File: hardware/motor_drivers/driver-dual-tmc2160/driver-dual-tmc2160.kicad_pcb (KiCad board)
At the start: 4 copper layers, 30 x 33.5 mm, 74 parts, among them M1 Micro-Fit 3.0, M2 Micro-Fit 3.0, Q1 DMHT6016LFJ, Q2 DMHT6016LFJ, Q3 DMHT6016LFJ, Q4 DMHT6016LFJ, T1 GND, T10 SCK, T11 GND, T12 DIR, T13 ENCB, T14 SDI, T15 EN, T16 ENCN, T17 SDO, T18 VCC, T2 CS0, T21 Therm, T3 DIAG0, T4 CLK, T5 STEP, T6 DIAG1, T7 12V, T8 GND, T9 ENCA, U1 TMC2160, U2 TMC2160

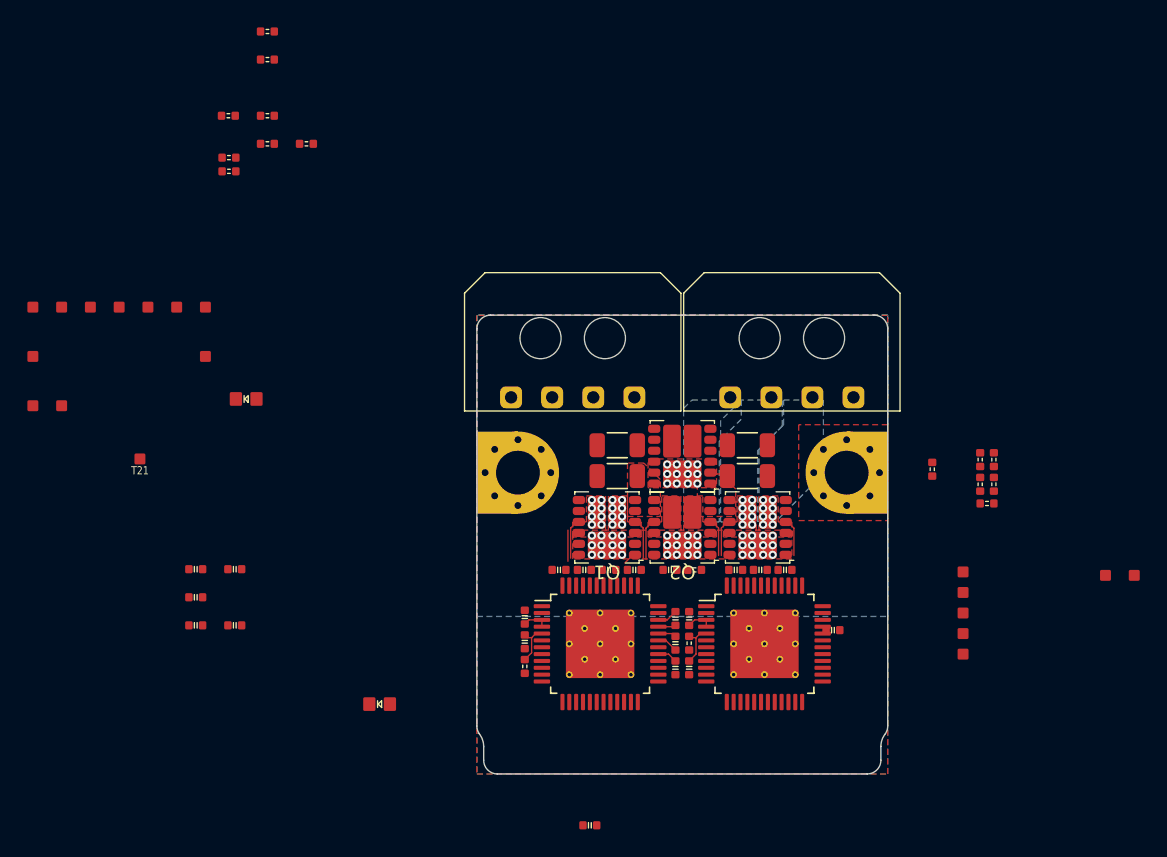
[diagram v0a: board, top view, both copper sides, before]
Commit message: added ctb v0.3 and dual 2160, fixed typo in v0.6 manual
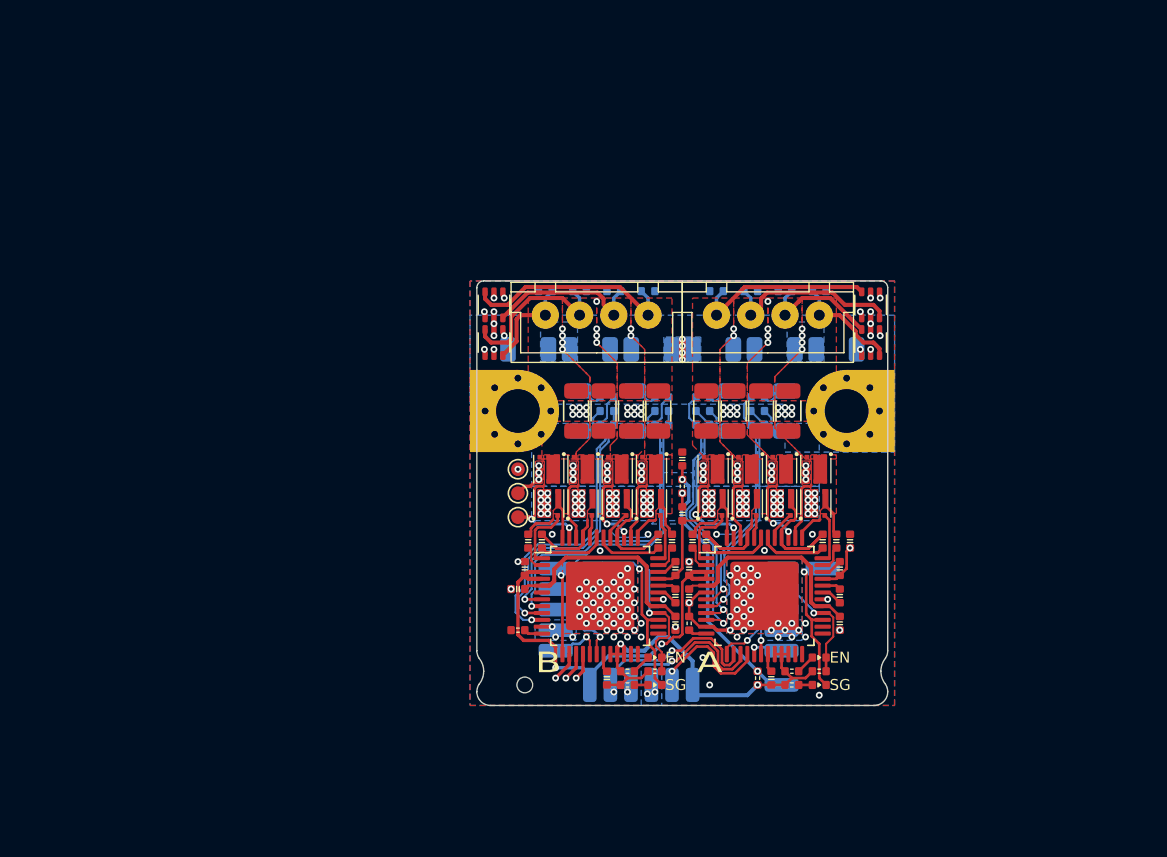
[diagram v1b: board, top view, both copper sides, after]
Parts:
- removed M1, M2: Micro-Fit 3.0, corevus:XKB_X3025WR-04
- removed T21: Therm, corevus:LGA_Land
- added C23: 100nF 100V, PCM_ME_passives:0402C, F.Cu at (134.5, 73.5)
- added C24: 1μF, PCM_ME_passives:0402C, F.Cu at (123.0, 73.0)
- added C25: 1µF, PCM_ME_passives:0402C, F.Cu at (134.5, 75.5)
- added C26: 1µF, PCM_ME_passives:0402C, F.Cu at (129.5, 79.5)
- added C27: 1μF, PCM_ME_passives:0402C, F.Cu at (123.5, 71.5)
- added C28: 100nF 100V, PCM_ME_passives:0402C, F.Cu at (135.0, 67.5)
- added C29: 1μF 25V, PCM_ME_passives:0402C, F.Cu at (123.8, 69.5)
- added C30: 1μF 25V, PCM_ME_passives:0402C, F.Cu at (124.8, 69.5)
- added C31: 1μF 25V, PCM_ME_passives:0402C, F.Cu at (133.2, 69.5)
- added C32: 1μF 25V, PCM_ME_passives:0402C, F.Cu at (134.2, 69.5)
- added C33: 1nF, PCM_ME_passives:0402C, B.Cu at (129.5, 61.0)
- added C34: 1nF 100V, PCM_ME_passives:0402C, B.Cu at (132.5, 51.2)
- added C35: 1nF 100V, PCM_ME_passives:0402C, B.Cu at (130.0, 51.2)
- added C36: 1nF 100V, PCM_ME_passives:0402C, B.Cu at (127.5, 51.2)
- added C37: 1nF 100V, PCM_ME_passives:0402C, B.Cu at (125.0, 51.2)
- added C38: 1μF 100V, Capacitor_SMD:C_1206_3216Metric, B.Cu at (137.2, 55.5)
- added C39: 1μF 100V, Capacitor_SMD:C_1206_3216Metric, B.Cu at (141.8, 55.5)
- added C40: 1μF 100V, Capacitor_SMD:C_1206_3216Metric, B.Cu at (146.2, 55.5)
- added C41: 1nF, PCM_ME_passives:0402C, B.Cu at (133.5, 61.0)
- added D3: BAV99S, Package_TO_SOT_SMD:SOT-363_SC-70-6, F.Cu at (148.8, 52.2)
- added D4: BAV99S, Package_TO_SOT_SMD:SOT-363_SC-70-6, F.Cu at (148.8, 55.0)
- added D5: Blu, PCM_ME_passives:0402LED, F.Cu at (133.0, 78.0)
- added D6: Ylw, PCM_ME_passives:0402LED, F.Cu at (133.0, 80.0)
- added D7: BAV99S, Package_TO_SOT_SMD:SOT-363_SC-70-6, F.Cu at (121.2, 52.2)
- added D8: BAV99S, Package_TO_SOT_SMD:SOT-363_SC-70-6, F.Cu at (121.2, 55.0)
- added FB1: 30Ω@100MHz, Resistor_SMD:R_1206_3216Metric, F.Cu at (142.8, 60.0)
- added FB2: 30Ω@100MHz, Resistor_SMD:R_1206_3216Metric, F.Cu at (140.8, 60.0)
- added FB3: 30Ω@100MHz, Resistor_SMD:R_1206_3216Metric, F.Cu at (138.8, 60.0)
- added FB4: 30Ω@100MHz, Resistor_SMD:R_1206_3216Metric, F.Cu at (136.8, 60.0)
- added FB5: 30Ω@100MHz, Resistor_SMD:R_1206_3216Metric, F.Cu at (133.2, 60.0)
- added FB6: 30Ω@100MHz, Resistor_SMD:R_1206_3216Metric, F.Cu at (131.2, 60.0)
- added FB7: 30Ω@100MHz, Resistor_SMD:R_1206_3216Metric, F.Cu at (129.2, 60.0)
- added FB8: 30Ω@100MHz, Resistor_SMD:R_1206_3216Metric, F.Cu at (127.2, 60.0)
- added H3: ToolingHole, corevus:ToolingHole, F.Cu at (123.5, 80.0)
- added J1: XH, corevus:JST_XH_1x04, F.Cu at (141.2, 53.0)
- added J2: XH, corevus:JST_XH_1x04, F.Cu at (128.8, 53.0)
- added NT1: NetTie_2, corevus:NetTie-2_SMD_Pad0.1mm, B.Cu at (137.8, 58.9)
- added NT2: NetTie_2, corevus:NetTie-2_SMD_Pad0.1mm, B.Cu at (141.8, 58.9)
- added NT3: NetTie_2, corevus:NetTie-2_SMD_Pad0.1mm, B.Cu at (128.2, 58.9)
- added NT4: NetTie_2, corevus:NetTie-2_SMD_Pad0.1mm, B.Cu at (132.2, 58.9)
- added Q10: DMT6016, corevus:DMT6016LFDF, F.Cu at (125.2, 64.2)
- added Q11: DMT6016, corevus:DMT6016LFDF, F.Cu at (127.8, 66.8)
- added Q12: DMT6016, corevus:DMT6016LFDF, F.Cu at (127.8, 64.2)
- added Q13: DMT6016, corevus:DMT6016LFDF, F.Cu at (130.2, 66.8)
- added Q14: DMT6016, corevus:DMT6016LFDF, F.Cu at (130.2, 64.2)
- added Q15: DMT6016, corevus:DMT6016LFDF, F.Cu at (132.8, 66.8)
- added Q16: DMT6016, corevus:DMT6016LFDF, F.Cu at (132.8, 64.2)
- added Q5: DMT6016, corevus:DMT6016LFDF, F.Cu at (142.2, 66.8)
- added Q6: DMT6016, corevus:DMT6016LFDF, F.Cu at (142.2, 64.2)
- added Q7: DMT6016, corevus:DMT6016LFDF, F.Cu at (144.8, 66.8)
- added Q8: DMT6016, corevus:DMT6016LFDF, F.Cu at (144.8, 64.2)
- added Q9: DMT6016, corevus:DMT6016LFDF, F.Cu at (125.2, 66.8)
- added R21: 47Ω, PCM_ME_passives:0402R, B.Cu at (133.5, 59.0)
- added T19: EN, corevus:LGA_Land_2.5mm, B.Cu at (125.8, 73.0)
- added TP1: TestPoint, TestPoint:TestPoint_Pad_D1.0mm, F.Cu at (123.0, 64.2)
- added TP5: TestPoint, TestPoint:TestPoint_Pad_D1.0mm, F.Cu at (123.0, 67.8)
- added TP6: TestPoint, TestPoint:TestPoint_Pad_D1.0mm, F.Cu at (123.0, 66.0)
- C1: value 100nF 16V -> 1μF 25V; footprint AlphaLib:0402C -> PCM_ME_passives:0402C
- C10, C11, C22, C8, C9: value 1μF -> 1μF 25V; footprint AlphaLib:0402C -> PCM_ME_passives:0402C
- C12: value 100nF 16V -> 1μF 100V; footprint AlphaLib:0402C -> Capacitor_SMD:C_1206_3216Metric; moved to B.Cu
- C13: value 22nF 100V -> 1μF; footprint AlphaLib:0402C -> PCM_ME_passives:0402C
- C14: value 1µF -> 1μF 100V; footprint AlphaLib:0402C -> Capacitor_SMD:C_1206_3216Metric; moved to B.Cu
- C15: value 1μF -> 1μF 100V; footprint AlphaLib:0402C -> Capacitor_SMD:C_1206_3216Metric; moved to B.Cu
- C16: value 1µF -> 1nF 100V; footprint AlphaLib:0402C -> PCM_ME_passives:0402C; moved to B.Cu
- C17, C19: value 1μF -> 1nF 100V; footprint AlphaLib:0402C -> PCM_ME_passives:0402C; moved to B.Cu
- C18: value 100nF 100V -> 1nF 100V; footprint AlphaLib:0402C -> PCM_ME_passives:0402C; moved to B.Cu
- C2: value 22nF 100V -> 100nF 100V; footprint AlphaLib:0402C -> PCM_ME_passives:0402C
- C20, C21: value 1μF -> 1nF; footprint AlphaLib:0402C -> PCM_ME_passives:0402C; moved to B.Cu
- C3, C4, C5, C6, C7: footprint AlphaLib:0402C -> PCM_ME_passives:0402C
- D1: value Red -> Blu; footprint AlphaLib:0603LED -> PCM_ME_passives:0402LED
- D2: value Red -> Ylw; footprint AlphaLib:0603LED -> PCM_ME_passives:0402LED
- Q1, Q2, Q3, Q4: value DMHT6016LFJ -> DMT6016; footprint corevus:V-DFN5045-12-Type-B -> corevus:DMT6016LFDF
- R1: value 1kΩ -> 4.7kΩ; footprint AlphaLib:0402R -> PCM_ME_passives:0402R
- R10, R13, R17: value 30mΩ -> 50mΩ; moved to B.Cu
- R11, R12, R15, R19, R8, R9: footprint AlphaLib:0402R -> PCM_ME_passives:0402R; moved to B.Cu
- R14: value 30mΩ -> 47Ω; footprint Resistor_SMD:R_1206_3216Metric -> PCM_ME_passives:0402R; moved to B.Cu
- R16: value 47Ω -> 1kΩ; footprint AlphaLib:0402R -> PCM_ME_passives:0402R
- R18: value 47Ω -> 50mΩ; footprint AlphaLib:0402R -> Resistor_SMD:R_1206_3216Metric; moved to B.Cu
- R2, R20, R3: footprint AlphaLib:0402R -> PCM_ME_passives:0402R
- R4: value 2.2Ω -> 10kΩ; footprint AlphaLib:0402R -> PCM_ME_passives:0402R
- R5: value 1kΩ -> 10kΩ; footprint AlphaLib:0402R -> PCM_ME_passives:0402R
- R6: value 10kΩ -> 4.7kΩ; footprint AlphaLib:0402R -> PCM_ME_passives:0402R
- R7: value 2.2Ω -> 1kΩ; footprint AlphaLib:0402R -> PCM_ME_passives:0402R
- T1: value GND -> DIAG; footprint corevus:LGA_Land -> corevus:LGA_Land_2.5mm; moved to B.Cu
- T10: value SCK -> CS0; footprint corevus:LGA_Land -> corevus:LGA_Land_2.5mm; moved to B.Cu
- T11: value GND -> STEP; footprint corevus:LGA_Land -> corevus:LGA_Land_2.5mm; moved to B.Cu
- T12: value DIR -> GND; footprint corevus:LGA_Land -> corevus:LGA_Land_2.5mm; moved to B.Cu
- T13: value ENCB -> DIR; footprint corevus:LGA_Land -> corevus:LGA_Land_2.5mm; moved to B.Cu
- T14: value SDI -> EN; footprint corevus:LGA_Land -> corevus:LGA_Land_2.5mm; moved to B.Cu
- T15: value EN -> STEP; footprint corevus:LGA_Land -> corevus:LGA_Land_2.5mm; moved to B.Cu
- T16: value ENCN -> GND; footprint corevus:LGA_Land -> corevus:LGA_Land_2.5mm; moved to B.Cu
- T17: value SDO -> DIAG; footprint corevus:LGA_Land -> corevus:LGA_Land_2.5mm; moved to B.Cu
- T18: value VCC -> DIR; footprint corevus:LGA_Land -> corevus:LGA_Land_2.5mm; moved to B.Cu
- T2: footprint corevus:LGA_Land -> corevus:LGA_Land_2.5mm; moved to B.Cu
- T3: value DIAG0 -> 12V; footprint corevus:LGA_Land -> corevus:LGA_Land_2.5mm; moved to B.Cu
- T4: value CLK -> SCK; footprint corevus:LGA_Land -> corevus:LGA_Land_2.5mm; moved to B.Cu
- T5: value STEP -> GND; footprint corevus:LGA_Land -> corevus:LGA_Land_2.5mm; moved to B.Cu
- T6: value DIAG1 -> SDI; footprint corevus:LGA_Land -> corevus:LGA_Land_2.5mm; moved to B.Cu
- T7: value 12V -> SDO; footprint corevus:LGA_Land -> corevus:LGA_Land_2.5mm; moved to B.Cu
- T8: value GND -> VCC; footprint corevus:LGA_Land -> corevus:LGA_Land_2.5mm; moved to B.Cu
- T9: value ENCA -> Therm; footprint corevus:LGA_Land -> corevus:LGA_Land_2.5mm; moved to B.Cu
- TH1: value 10kΩ 3380K -> 10kΩ 3950K; footprint AlphaLib:0402R -> PCM_ME_passives:0402R
- moved T17 58.9 mm to (145.2, 71.5), turned to -90 degrees
- moved R1 57.8 mm to (143.0, 79.0)
- moved R2 57.1 mm to (145.0, 79.0)
- moved T8 53.8 mm to (135.8, 80.0)
- moved R6 51.8 mm to (131.0, 79.0)
- moved R5 47.4 mm to (123.0, 76.0), turned to 180 degrees
- moved C16 47.3 mm to (145.0, 51.2), turned to 180 degrees
- moved R3 47.1 mm to (135.5, 75.5), turned to 90 degrees
- moved T5 46.0 mm to (132.8, 80.0)
- moved D1 45.9 mm to (145.0, 78.0), turned to 180 degrees
- moved T3 45.7 mm to (128.2, 80.0)
- moved T1 45.4 mm to (128.8, 71.5), turned to -90 degrees
- moved T4 45.2 mm to (129.8, 80.0)
- moved C18 44.9 mm to (140.0, 51.2), turned to 180 degrees
- moved T7 43.8 mm to (134.2, 80.0)
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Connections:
- C10 pad 2: /_{M0}A1 -> /_{MA}A1
- C11 pad 2: /_{M0}A2 -> /_{MA}A2
- C12 pad 1: Net-(U2-VCP) -> +48V
- C12 pad 2: +48V -> GND
- C13 pad 1: Net-(U2-CPO) -> /THERM
- C13 pad 2: Net-(U2-CPI) -> GND
- C14 pad 1: GND -> +48V
- C14 pad 2: VCC -> GND
- C15 pad 1: GND -> +48V
- C15 pad 2: Net-(U2-5VOUT) -> GND
- C16 pad 2: Net-(U2-VCC) -> /_{MA}A2'
- C17 pad 1: +12V -> GND
- C17 pad 2: GND -> /_{MA}A1'
- C18 pad 1: +48V -> GND
- C18 pad 2: GND -> /_{MA}B2'
- C19 pad 1: Net-(U2-CB1) -> GND
- C19 pad 2: /_{M1}B1 -> /_{MA}B1'
- C20 pad 1: Net-(U2-CB2) -> /_{MA}SRBL
- C20 pad 2: /_{M1}B2 -> /_{MA}SRBH
- C21 pad 1: Net-(U2-CA1) -> /_{MA}SRAL
- C21 pad 2: /_{M1}A1 -> /_{MA}SRAH
- C22 pad 1: Net-(U2-CA2) -> Net-(U2-VCP)
- C22 pad 2: /_{M1}A2 -> +48V
- C5 pad 2: Net-(U1-VCC) -> Net-(U1-5VOUT)
- C8 pad 2: /_{M0}B1 -> /_{MA}B1
- C9 pad 2: /_{M0}B2 -> /_{MA}B2
- D1 pad 1: Net-(D1-K) -> /_{MA}~{En}
- D1 pad 2: VCC -> Net-(D1-A)
- D2 pad 1: Net-(D2-K) -> /_{MA}Stall
- D2 pad 2: VCC -> Net-(D2-A)
- Q1 pad 1: /_{M0}HA1 -> +48V
- Q1 pad 3: /_{M0}A1 -> /_{MA}HB1
- Q1 pad 4: /_{M0}LA1 -> /_{MA}B1
- Q1 pad 5: Net-(Q1-S2-Pad5) -> +48V
- Q1 pad 6: Net-(Q1-S2-Pad5) -> +48V
- Q1 pad 7: Net-(Q1-S3-Pad7) -> /_{MA}B1
- Q1 pad 8: Net-(Q1-S3-Pad7) -> +48V
- Q2 pad 1: /_{M1}HB1 -> /_{MA}B1
- Q2 pad 2: +48V -> /_{MA}B1
- Q2 pad 3: /_{M1}B1 -> /_{MA}LB1
- Q2 pad 4: /_{M1}LB1 -> Net-(Q2-S-Pad4)
- Q2 pad 5: Net-(Q2-S2-Pad5) -> /_{MA}B1
- Q2 pad 6: Net-(Q2-S2-Pad5) -> /_{MA}B1
- Q2 pad 7: Net-(Q1-S2-Pad5) -> Net-(Q2-S-Pad4)
- Q2 pad 8: Net-(Q1-S2-Pad5) -> /_{MA}B1
- Q3 pad 1: /_{M1}HA2 -> +48V
- Q3 pad 3: /_{M1}A2 -> /_{MA}HB2
- Q3 pad 4: /_{M1}LA2 -> /_{MA}B2
- Q3 pad 5: Net-(Q3-S2-Pad5) -> +48V
- Q3 pad 6: Net-(Q3-S2-Pad5) -> +48V
- Q3 pad 7: Net-(Q1-S3-Pad7) -> /_{MA}B2
- Q3 pad 8: Net-(Q1-S3-Pad7) -> +48V
- Q4 pad 1: /_{M1}HA1 -> /_{MA}B2
- Q4 pad 2: +48V -> /_{MA}B2
- Q4 pad 3: /_{M1}A1 -> /_{MA}LB2
- Q4 pad 4: /_{M1}LA1 -> Net-(Q2-S-Pad4)
- Q4 pad 5: Net-(Q3-S2-Pad5) -> /_{MA}B2
- Q4 pad 6: Net-(Q3-S2-Pad5) -> /_{MA}B2
- Q4 pad 7: Net-(Q2-S2-Pad5) -> Net-(Q2-S-Pad4)
- Q4 pad 8: Net-(Q2-S2-Pad5) -> /_{MA}B2
- R1 pad 1: Net-(D1-K) -> VCC
- R1 pad 2: /_{M0}~{En} -> Net-(D1-A)
- R10 pad 1: Net-(Q1-S3-Pad7) -> Net-(Q2-S-Pad4)
- R11 pad 1: Net-(Q1-S2-Pad5) -> Net-(Q6-S-Pad4)
- R11 pad 2: /_{M0}SRAH -> /_{MA}SRAH
- R12 pad 1: GND -> Net-(NT2-Pad2)
- R12 pad 2: /_{M0}SRAL -> /_{MA}SRAL
- R13 pad 1: Net-(Q1-S2-Pad5) -> Net-(Q6-S-Pad4)
- R14 pad 1: Net-(Q2-S2-Pad5) -> Net-(Q10-S-Pad4)
- R14 pad 2: GND -> /_{MB}SRBH
- R15 pad 1: Net-(Q2-S2-Pad5) -> Net-(NT3-Pad1)
- R15 pad 2: /_{M1}SRBH -> /_{MB}SRBL
- R16 pad 1: GND -> VCC
- R16 pad 2: /_{M1}SRBL -> Net-(D2-A)
- R17 pad 1: Net-(Q3-S2-Pad5) -> Net-(Q10-S-Pad4)
- R18 pad 1: Net-(Q3-S2-Pad5) -> Net-(Q14-S-Pad4)
- R18 pad 2: /_{M1}SRAH -> GND
- R19 pad 1: GND -> Net-(Q14-S-Pad4)
- R19 pad 2: /_{M1}SRAL -> /_{MB}SRAH
- R2 pad 2: /_{M0}~{En} -> /_{MA}~{En}
- R3 pad 1: /Clk -> Net-(U1-CLK)
- R4 pad 1: Net-(U1-5VOUT) -> VCC
- R4 pad 2: Net-(U1-VCC) -> /_{MB}~{En}
- R5 pad 1: Net-(D2-K) -> Net-(U2-CLK)
- R5 pad 2: /_{M1}~{En} -> GND
- R6 pad 2: /_{M1}~{En} -> Net-(D5-A)
- R7 pad 1: Net-(U2-5VOUT) -> VCC
- R7 pad 2: Net-(U2-VCC) -> Net-(D6-A)
- R8 pad 1: Net-(Q1-S3-Pad7) -> Net-(Q2-S-Pad4)
- R8 pad 2: /_{M0}SRBH -> /_{MA}SRBH
- R9 pad 1: GND -> Net-(NT1-Pad1)
- R9 pad 2: /_{M0}SRBL -> /_{MA}SRBL
- T1 pad 1: GND -> /_{MB}Stall
- T10 pad 1: /SCK -> /_{MA}~{CS}
- T11 pad 1: GND -> /_{MA}Step
- T12 pad 1: /Dir -> GND
- T13 pad 1: /ENCB -> /_{MA}Dir
- T14 pad 1: /SDI -> /_{MA}~{En}
- T15 pad 1: /~{En} -> /_{MB}Step
- T16 pad 1: /ENCN -> GND
- T17 pad 1: /SDO -> /_{MA}Stall
- T18 pad 1: VCC -> /_{MB}Dir
- T2 pad 1: /~{CS} -> /_{MB}~{CS}
- T3 pad 1: /Diag0 -> +12V
- T4 pad 1: /Clk -> /SCK
- T5 pad 1: /Step -> GND
- T6 pad 1: /Diag1 -> /SDI
- T7 pad 1: +12V -> /SDO
- T8 pad 1: GND -> VCC
- T9 pad 1: /ENCA -> /THERM
- U1 pad 1: /_{M0}HB1 -> /_{MA}HB1
- U1 pad 10: /_{M0}SRBL -> /_{MA}SRBL
- U1 pad 12: /Clk -> Net-(U1-CLK)
- U1 pad 13: /~{CS} -> /_{MA}~{CS}
- U1 pad 17: /_{M0}Step -> /_{MA}Step
- U1 pad 18: /_{M0}Dir -> /_{MA}Dir
- U1 pad 26: /_{M0}Stall -> unconnected-(U1-DIAG0-Pad26)
- U1 pad 27: unconnected-(U1-DIAG1-Pad27) -> /_{MA}Stall
- U1 pad 28: /_{M0}~{En} -> /_{MA}~{En}
- U1 pad 29: Net-(U1-VCC) -> Net-(U1-5VOUT)
- U1 pad 36: /_{M0}HA2 -> /_{MA}HA2
- U1 pad 37: /_{M0}A2 -> /_{MA}A2
- U1 pad 38: /_{M0}LA2 -> /_{MA}LA2
- U1 pad 39: /_{M0}LA1 -> /_{MA}LA1
- U1 pad 40: /_{M0}A1 -> /_{MA}A1
- U1 pad 41: /_{M0}HA1 -> /_{MA}HA1
- U1 pad 44: /_{M0}HB2 -> /_{MA}HB2
- U1 pad 45: /_{M0}B2 -> /_{MA}B2
- U1 pad 46: /_{M0}LB2 -> /_{MA}LB2
- U1 pad 47: /_{M0}LB1 -> /_{MA}LB1
- U1 pad 48: /_{M0}B1 -> /_{MA}B1
- U1 pad 7: /_{M0}SRAL -> /_{MA}SRAL
- U1 pad 8: /_{M0}SRAH -> /_{MA}SRAH
- U1 pad 9: /_{M0}SRBH -> /_{MA}SRBH
- U2 pad 1: /_{M1}HB1 -> /_{MB}HB1
- U2 pad 10: /_{M1}SRBL -> /_{MB}SRBL
- U2 pad 12: /Clk -> Net-(U2-CLK)
- U2 pad 13: /~{CS} -> /_{MB}~{CS}
- U2 pad 17: /_{M1}Step -> /_{MB}Step
- U2 pad 18: /_{M1}Dir -> /_{MB}Dir
- U2 pad 26: /_{M1}Stall -> unconnected-(U2-DIAG0-Pad26)
- U2 pad 27: unconnected-(U2-DIAG1-Pad27) -> /_{MB}Stall
- U2 pad 28: /_{M1}~{En} -> /_{MB}~{En}
- U2 pad 29: Net-(U2-VCC) -> Net-(U2-5VOUT)
- U2 pad 36: /_{M1}HA2 -> /_{MB}HA2
- U2 pad 37: /_{M1}A2 -> /_{MB}A2
- U2 pad 38: /_{M1}LA2 -> /_{MB}LA2
- U2 pad 39: /_{M1}LA1 -> /_{MB}LA1
- U2 pad 40: /_{M1}A1 -> /_{MB}A1
- U2 pad 41: /_{M1}HA1 -> /_{MB}HA1
- U2 pad 44: /_{M1}HB2 -> /_{MB}HB2
- U2 pad 45: /_{M1}B2 -> /_{MB}B2
- U2 pad 46: /_{M1}LB2 -> /_{MB}LB2
- U2 pad 47: /_{M1}LB1 -> /_{MB}LB1
- U2 pad 48: /_{M1}B1 -> /_{MB}B1
- U2 pad 7: /_{M1}SRAL -> /_{MB}SRAL
- U2 pad 8: /_{M1}SRAH -> /_{MB}SRAH
- U2 pad 9: /_{M1}SRBH -> /_{MB}SRBH
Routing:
- net VCC: track 0.00 -> 29.3 mm, vias 0 -> 2
- net +12V: track 3.79 -> 31.0 mm, vias 0 -> 2
- net /_{MB}SRAL: track 0.00 -> 24.9 mm, vias 0 -> 1
- net /_{MB}SRAH: track 0.00 -> 23.4 mm, vias 0 -> 1
- net /_{MB}SRBL: track 0.00 -> 23.0 mm, vias 0 -> 1
- net /_{MB}SRBH: track 0.00 -> 20.8 mm, vias 0 -> 1
- net /_{MA}SRBL: track 0.00 -> 20.0 mm, vias 0 -> 1
- net /THERM: track 0.00 -> 19.9 mm, vias 0 -> 2
- net GND: track 0.00 -> 19.3 mm, vias 0 -> 137
- net /SCK: track 0.00 -> 18.9 mm, vias 0 -> 3
- net /SDO: track 0.00 -> 18.5 mm, vias 0 -> 2
- net /SDI: track 0.00 -> 18.1 mm, vias 0 -> 3
- net /_{MA}SRBH: track 0.00 -> 17.9 mm, vias 0 -> 1
- net /_{MB}~{En}: track 0.00 -> 17.6 mm, vias 0 -> 1
- net /_{MA}SRAL: track 0.00 -> 17.3 mm, vias 0 -> 1
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- added copper zone on In2.Cu, net +48V
- added copper zone on In3.Cu, net +48V
- added copper zone on F.Cu, net /_{MA}A1
- added copper zone on F.Cu, net /_{MA}A1'
- added copper zone on F.Cu, net /_{MA}A2
- added copper zone on F.Cu, net /_{MA}A2'
- added copper zone on F.Cu, net /_{MA}B1
- added copper zone on F.Cu, net /_{MA}B1'
- added copper zone on F.Cu, net /_{MA}B2
- added copper zone on F.Cu, net /_{MA}B2'
- added copper zone on F.Cu, net /_{MB}A1
- added copper zone on F.Cu, net /_{MB}A1'
- added copper zone on F.Cu, net /_{MB}A2
- added copper zone on F.Cu, net /_{MB}A2'
- added copper zone on F.Cu, net /_{MB}B1
- added copper zone on F.Cu, net /_{MB}B1'
- added copper zone on F.Cu, net /_{MB}B2
- added copper zone on F.Cu, net /_{MB}B2'
- added copper zone on In3.Cu, net GND
- added copper zone on In4.Cu, net GND
- added copper zone on B.Cu, net Net-(Q10-S-Pad4)
- added copper zone on F.Cu, net Net-(Q10-S-Pad4)
- added copper zone on B.Cu, net Net-(Q14-S-Pad4)
- added copper zone on F.Cu, net Net-(Q14-S-Pad4)
- added copper zone on B.Cu, net Net-(Q2-S-Pad4)
- added copper zone on F.Cu, net Net-(Q2-S-Pad4)
- added copper zone on B.Cu, net Net-(Q6-S-Pad4)
- added copper zone on F.Cu, net Net-(Q6-S-Pad4)
- removed copper zone on F.Cu, net +48V
- removed copper zone on F.Cu, net /_{M0}A1
- removed copper zone on F.Cu, net /_{M0}A2
- removed copper zone on F.Cu, net /_{M0}B2
- removed copper zone on B.Cu, net /_{M1}A1
- removed copper zone on F.Cu, net /_{M1}A1
- removed copper zone on B.Cu, net /_{M1}B1
- removed copper zone on F.Cu, net /_{M1}B1
- removed copper zone on B.Cu, net /_{M1}B2
- removed copper zone on F.Cu, net /_{M1}B2
- removed copper zone on F.Cu, net Net-(Q1-S2-Pad5)
- removed copper zone on F.Cu, net Net-(Q2-S2-Pad5)
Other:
- board size 30 x 33.5 mm -> 30 x 31 mm
- copper layers 4 -> 6
- board text added: "12V"
- board text added: "3V3"
- board text added: "A"
- board text added: "B"
- board text added: "CS"
- board text added: "DIR"
- board text added: "EN"
- board text added: "GND"
- board text added: "MISO"
- board text added: "MOSI"
- board text added: "NOT FOR PRODUCTION USE MERIDI ENGINEERING JULY 2024 DUAL TMC2160 STEPPER DRIVER MODULE 48V MAX / ???Arms MAX PER DRIVER"
- board text added: "SCLK"
- board text added: "SG"
- board text added: "STALL"
- board text added: "STEP"
- board text added: "THERM"

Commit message: last before i go on v0.7
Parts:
- removed H3: ToolingHole, corevus:ToolingHole
- added H4: ToolingHole, corevus:ToolingHole, F.Cu at (0.65, 0.65)
- D1, D5: value Blu -> Grn
- moved C17 5.15 mm to (147.5, 52.5), turned to 180 degrees
- moved C36 5.15 mm to (122.5, 52.5), turned to 0 degrees
- moved C18 4.25 mm to (140.0, 55.5), turned to 90 degrees
- moved C35 4.25 mm to (130.0, 55.5), turned to 90 degrees
- moved C16 3.36 mm to (147.5, 53.5)
- moved C19 3.36 mm to (135.0, 53.5)
- moved C37 3.36 mm to (122.5, 53.5)
- moved C34 2.80 mm to (135.0, 52.5)
- moved C12 1.00 mm to (122.8, 55.5)
- moved C14 1.00 mm to (127.2, 55.5)
- moved C39 1.00 mm to (142.8, 55.5)
- moved C40 1.00 mm to (147.2, 55.5)
- moved C1 0.25 mm to (146.5, 71.8)
- moved C10 0.25 mm to (145.2, 69.8)
- moved C11 0.25 mm to (146.2, 69.8)
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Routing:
- net GND: track 19.3 -> 8.31 mm, vias 137 -> 139
- net /_{MA}A1': track 9.03 -> 12.4 mm
- net /_{MB}B1': track 7.25 -> 3.86 mm
- net /_{MB}B2': track 12.4 -> 15.3 mm
- net /_{MA}A2': track 8.03 -> 5.42 mm
- net /_{MB}~{En}: track 17.6 -> 15.5 mm
- net /_{MA}Stall: track 10.1 -> 11.6 mm
- net +48V: track 17.9 -> 19.1 mm, vias 87 -> 83
- net /_{MB}A1': track 10.7 -> 11.8 mm
- net /_{MA}B2': track 12.6 -> 13.3 mm
- net /_{MB}~{CS}: track 5.79 -> 6.53 mm
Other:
- board text added: "DUAL TMC2160 48V xA EVALUATION USE ONLY"
- board text added: "NOT FOR PRODUCTION USE MERIDI ENGINEERING JULY 2024 DUAL TMC2160 STEPPER DRIVER MODULE 48V MAX xArms MAX PER DRIVER"
- board text added: "corevus"
- board text removed: "NOT FOR PRODUCTION USE MERIDI ENGINEERING JULY 2024 DUAL TMC2160 STEPPER DRIVER MODULE 48V MAX / ???Arms MAX PER DRIVER"

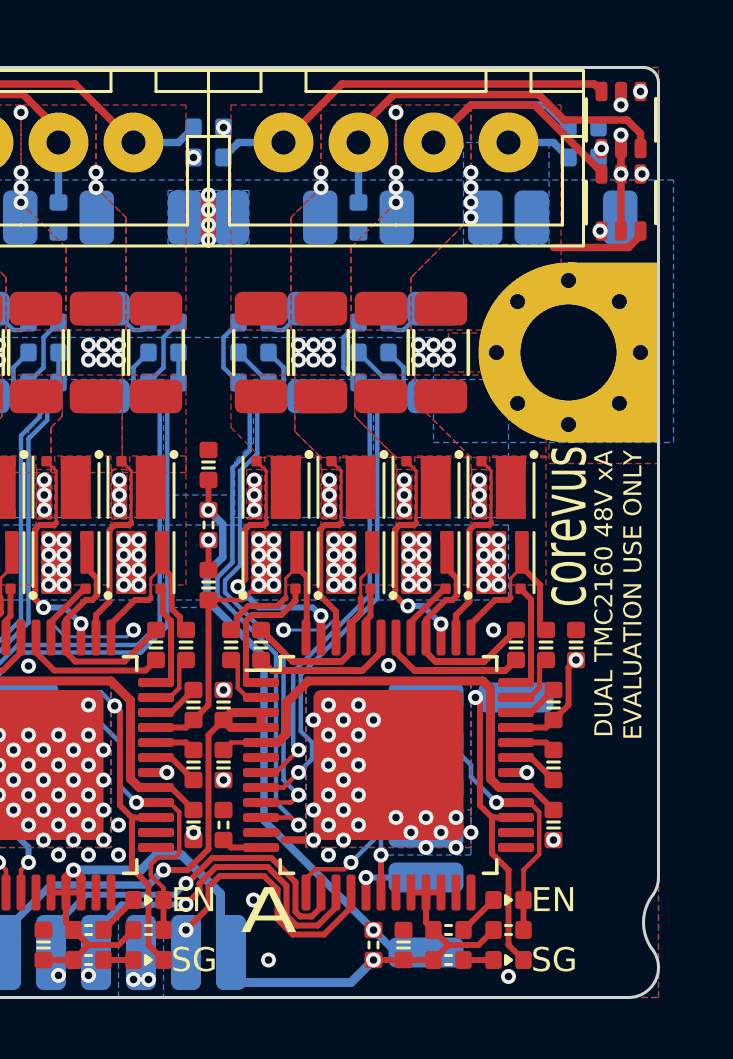
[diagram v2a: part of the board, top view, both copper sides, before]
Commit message: 48v extruder driver first prototype, dual tmc2160 polish for next rev
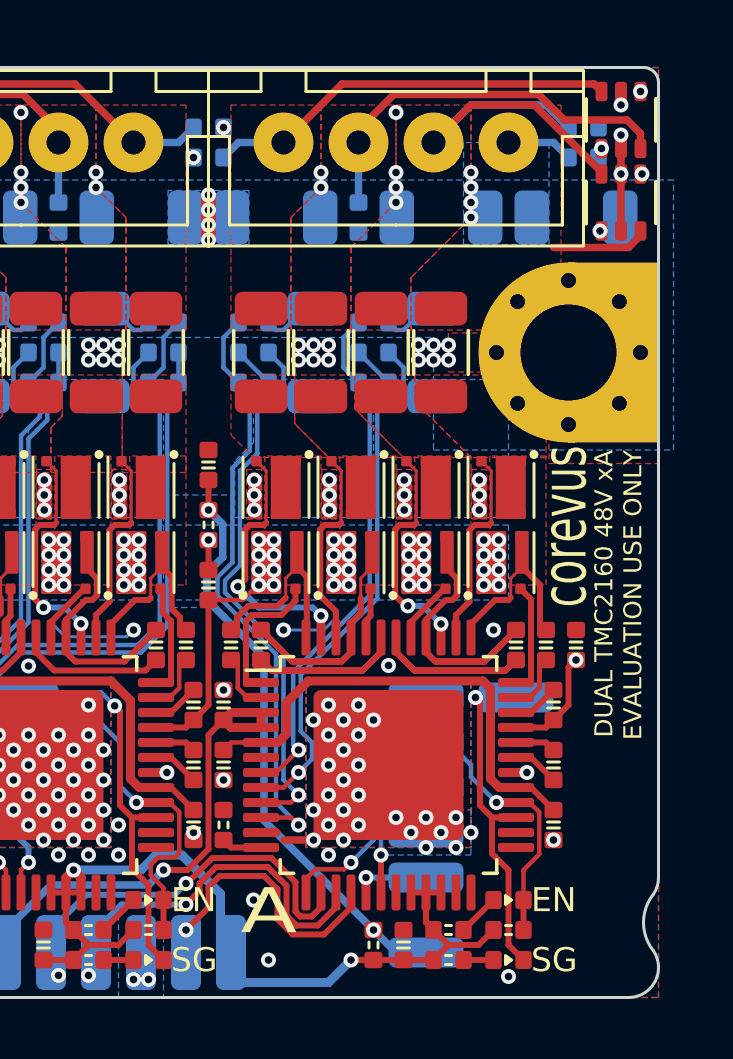
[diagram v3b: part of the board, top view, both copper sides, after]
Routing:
- net VCC: track 28.9 -> 29.7 mm
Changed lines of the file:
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@@
 	)
 	(segment
-		(start 140.5 80.250001)
-		(end 140.5 80.25)
-		(width 0.2)
-		(layer "F.Cu")
-		(net 19)
-	)
-	(segment
 		(start 130.75 78.000001)
 		(end 130.75 77.500001)
@@
 	)
 	(segment
+		(start 139.75 80.25)
+		(end 140.5 80.25)
+		(width 0.2)
+		(layer "F.Cu")
+		(net 19)
+	)
+	(segment
 		(start 141.5 80.25)
 		(end 142.499999 80.25)
@@
 	)
 	(segment
-		(start 141.5 80.25)
-		(end 140.5 80.250001)
+		(start 130.25 78.000001)
+		(end 130.75 78.000001)
 		(width 0.2)
 		(layer "F.Cu")
@@
 	)
 	(segment
-		(start 130.25 78.000001)
-		(end 130.75 78.000001)
+		(start 141.5 80.25)
+		(end 139.75 80.25)
 		(width 0.2)
 		(layer "F.Cu")
@@
 	)
 	(via
-		(at 140.5 80.250001)
+		(at 139.75 80.25)
 		(size 0.5)
 		(drill 0.25)
@@
 	)
 	(segment
-		(start 140.5 80.250001)
-		(end 139.75 81.000001)
-		(width 0.3)
-		(layer "B.Cu")
-		(net 19)
-	)
-	(segment
-		(start 139.75 81.000001)
-		(end 135.75 81.000001)
-		(width 0.3)
-		(layer "B.Cu")
-		(net 19)
-	)
-	(segment
 		(start 130.5 77.250001)
 		(end 132.75 77.250001)
@@
 	)
 	(segment
+		(start 138.999999 81.000001)
+		(end 135.75 81.000001)
+		(width 0.3)
+		(layer "B.Cu")
+		(net 19)
+	)
+	(segment
 		(start 133.250001 76.75)
 		(end 134.107107 76.75)
@@
 	)
 	(segment
+		(start 139.75 80.25)
+		(end 138.999999 81.000001)
+		(width 0.3)
+		(layer "B.Cu")
+		(net 19)
+	)
+	(segment
 		(start 132.75 77.250001)
 		(end 133.250001 76.75)
@@
 		(polygon
 			(pts
-				(xy 139.875 60.75) (xy 137.875 60.75) (xy 137.875 62.625) (xy 138.75 63.5) (xy 141.25 63.5) (xy 139.875 62.125)
+				(xy 139.875 60.75) (xy 137.875 60.75) (xy 137.875 62.375) (xy 139 63.5) (xy 141.5 63.5) (xy 139.875 61.875)
 			)
 		)
@@
 		(polygon
 			(pts
-				(xy 141.875 60.75) (xy 139.875 60.75) (xy 139.875 62.125) (xy 141.25 63.5) (xy 143.75 63.5) (xy 141.875 61.625)
+				(xy 141.875 60.75) (xy 139.875 60.75) (xy 139.875 61.875) (xy 141.5 63.5) (xy 143.75 63.5) (xy 141.875 61.625)
 			)
 		)
@@
 		(polygon
 			(pts
-				(xy 137.875 60.75) (xy 135.75 60.75) (xy 135.75 62.5) (xy 136.75 63.5) (xy 138.75 63.5) (xy 137.875 62.625)
+				(xy 137.875 60.75) (xy 135.75 60.75) (xy 135.75 62.75) (xy 136.5 63.5) (xy 139 63.5) (xy 137.875 62.375)
 			)
 		)
@@
 		(priority 10)
 		(connect_pads yes
-			(clearance 0.15)
+			(clearance 0.1)
 		)
 		(min_thickness 0.1)
@@
 		(polygon
 			(pts
-				(xy 119.5 54.25) (xy 119.5 59.5) (xy 142.5 59.5) (xy 142.5 63) (xy 150.5 63) (xy 150.5 54.25)
+				(xy 119.5 54.25) (xy 119.5 59.5) (xy 142.5 59.5) (xy 142.5 63.25) (xy 150.5 63.25) (xy 150.5 54.25)
 			)
 		)
